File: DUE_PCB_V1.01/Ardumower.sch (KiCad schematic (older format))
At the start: 57 parts, among them J1 I2C_1, J10 P_Left, J11 P_Right, J12 Sonar_R, J13 Sonar_C, J14 Sonar_L, J15 Bumper, J16 Button, J17 Button, J18 Button, J19 Button, J2 I2C_2, J20 5V IN, J21 Remote, J22 PCB_2, J23 5V, J24 3.3V IN, J25 3.3V, J26 GND, J27 RX & TX, J3 I2C_3, J4 DS3231 RTC, J5 9V IN, J6 Drop_Left, J7 Drop_Right, J8 Tilt, J9 Rain

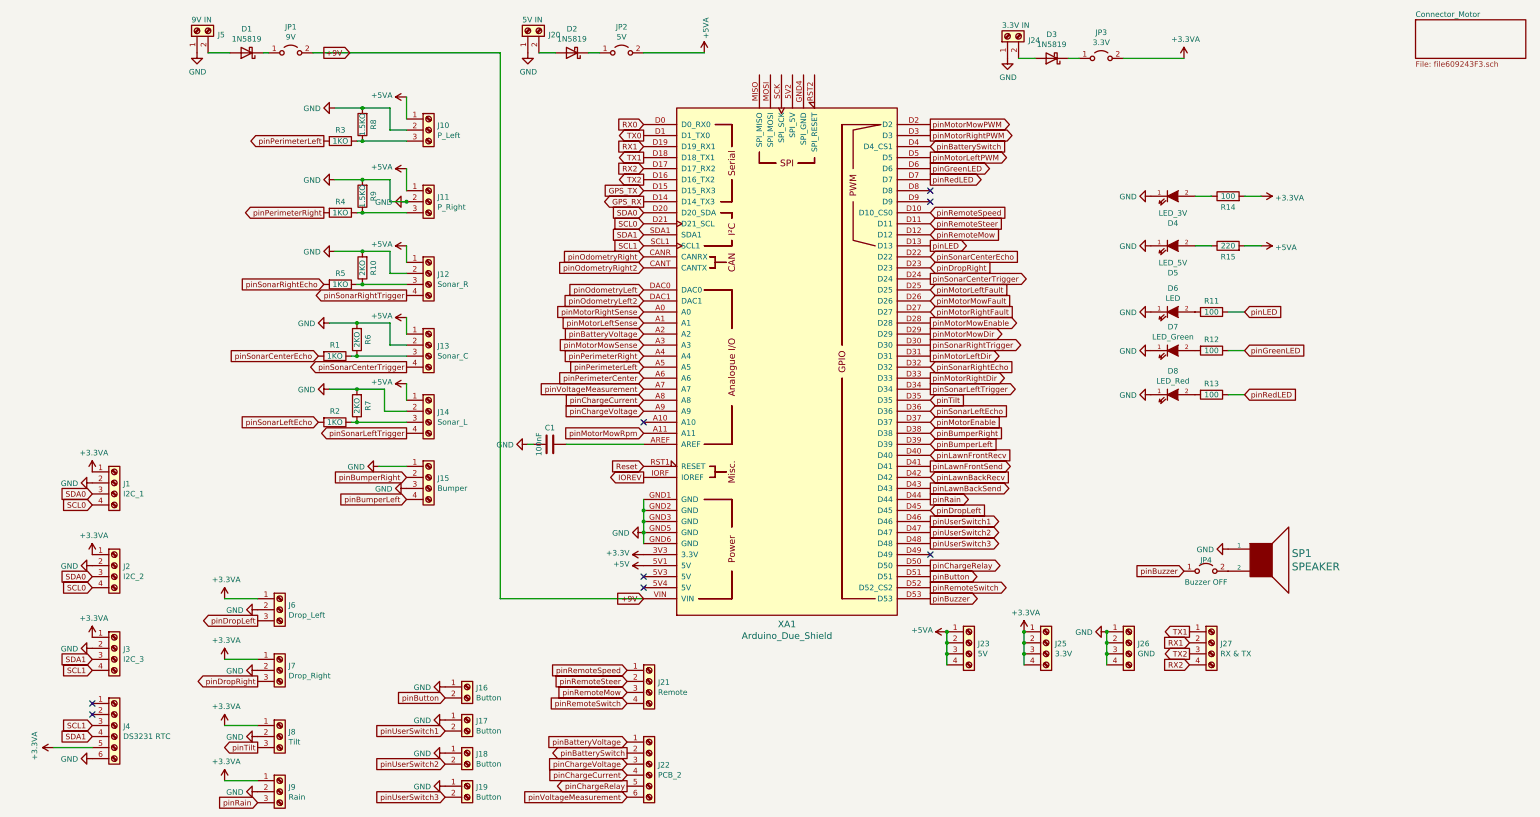
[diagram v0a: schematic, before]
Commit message: Add Power Connector for 5V and 3.3V
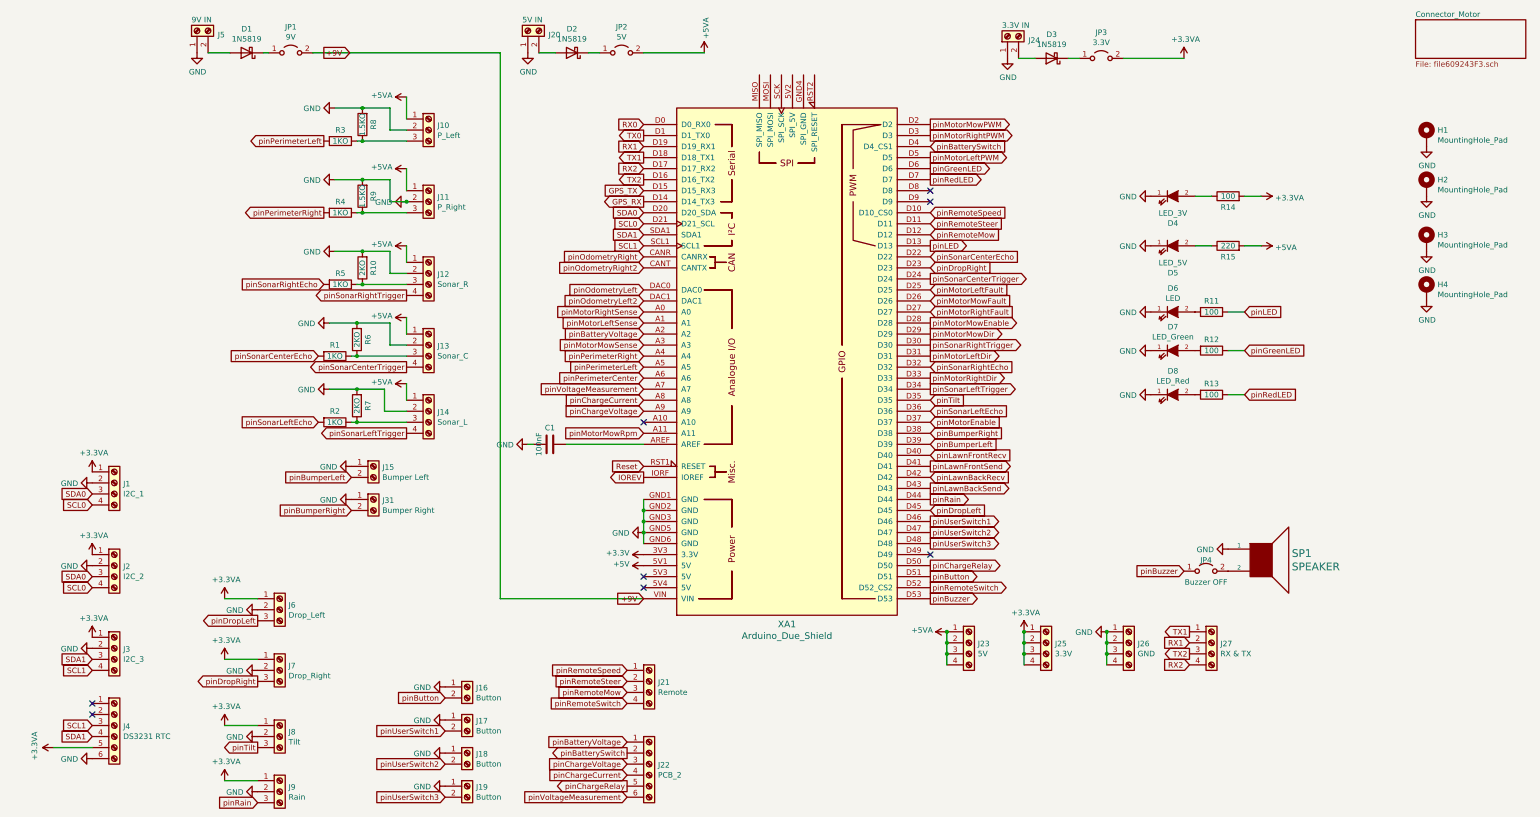
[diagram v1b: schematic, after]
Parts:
- removed J15: Bumper, Connector_PinHeader_2.54mm:PinHeader_1x04_P2.54mm_Vertical, symbol Connector:Screw_Terminal_01x04
- added H1, H2, H3, H4: MountingHole_Pad, MountingHole:MountingHole_2.2mm_M2_Pad_TopBottom, symbol Mechanical:MountingHole_Pad
- added J15: Bumper Left, Zimprich:Pin_Header_KK110_1x02_3D, symbol Connector:Screw_Terminal_01x02
- added J31: Bumper Right, Zimprich:Pin_Header_KK110_1x02_3D, symbol Connector:Screw_Terminal_01x02
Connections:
- net GND: now also H1.1, H2.1, H3.1, H4.1, J15.1 (Pin_1), J31.1 (Pin_1)
- net pinBumperLeft: now also J15.2 (Pin_2)
- net pinBumperRight: now also J31.2 (Pin_2)
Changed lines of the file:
@@
 Text GLabel 1900 4200 0    50   Input ~ 0
 pinSonarLeftEcho
-$Comp
-L Connector:Screw_Terminal_01x04 J15
-U 1 1 60770CE6
-P 2900 4700
-F 0 "J15" H 2980 4692 50  0000 L CNN
-F 1 "Bumper" H 2980 4601 50  0000 L CNN
-F 2 "Connector_PinHeader_2.54mm:PinHeader_1x04_P2.54mm_Vertical" H 2900 4700 50  0001 C CNN
-F 3 "~" H 2900 4700 50  0001 C CNN
-	1    2900 4700
-	1    0    0    -1
-$EndComp
-Text GLabel 2700 4700 0    50   Input ~ 0
+Text GLabel 2200 5000 0    50   Input ~ 0
 pinBumperRight
-Text GLabel 2700 4900 0    50   Input ~ 0
+Text GLabel 2200 4700 0    50   Input ~ 0
 pinBumperLeft
 $Comp
@@
 $EndComp
 $Comp
-L power:GND #PWR023
-U 1 1 6097EBFF
-P 2450 4600
-F 0 "#PWR023" H 2450 4350 50  0001 C CNN
-F 1 "GND" V 2455 4472 50  0000 R CNN
-F 2 "" H 2450 4600 50  0001 C CNN
-F 3 "" H 2450 4600 50  0001 C CNN
-	1    2450 4600
-	0    1    1    0
-$EndComp
-$Comp
 L power:GND #PWR018
 U 1 1 6097F3DC
@@
 	1    800  850
 	1    0    0    -1
-$EndComp
-Wire Wire Line
-	2450 4600 2700 4600
-$Comp
-L power:GND #PWR030
-U 1 1 609BE8A2
-P 2700 4800
-F 0 "#PWR030" H 2700 4550 50  0001 C CNN
-F 1 "GND" V 2705 4672 50  0000 R CNN
-F 2 "" H 2700 4800 50  0001 C CNN
-F 3 "" H 2700 4800 50  0001 C CNN
-	1    2700 4800
-	0    1    1    0
 $EndComp
 $Comp
@@
 	0    1    1    0
 $EndComp
+$Comp
+L Mechanical:MountingHole_Pad H2
+U 1 1 6091DE79
+P 11950 2050
+F 0 "H2" H 12050 2099 50  0000 L CNN
+F 1 "MountingHole_Pad" H 12050 2008 50  0000 L CNN
+F 2 "MountingHole:MountingHole_2.2mm_M2_Pad_TopBottom" H 11950 2050 50  0001 C CNN
+F 3 "~" H 11950 2050 50  0001 C CNN
+	1    11950 2050
+	1    0    0    -1
+$EndComp
+$Comp
+L power:GND #PWR055
+U 1 1 609238F5
+P 11950 2150
+F 0 "#PWR055" H 11950 1900 50  0001 C CNN
+F 1 "GND" H 11955 1977 50  0000 C CNN
+F 2 "" H 11950 2150 50  0001 C CNN
+F 3 "" H 11950 2150 50  0001 C CNN
+	1    11950 2150
+	1    0    0    -1
+$EndComp
+$Comp
+L Mechanical:MountingHole_Pad H1
+U 1 1 6092EAEB
+P 11950 1600
+F 0 "H1" H 12050 1649 50  0000 L CNN
+F 1 "MountingHole_Pad" H 12050 1558 50  0000 L CNN
+F 2 "MountingHole:MountingHole_2.2mm_M2_Pad_TopBottom" H 11950 1600 50  0001 C CNN
+F 3 "~" H 11950 1600 50  0001 C CNN
+	1    11950 1600
+	1    0    0    -1
+$EndComp
+$Comp
+L power:GND #PWR054
+U 1 1 6092F555
+P 11950 1700
+F 0 "#PWR054" H 11950 1450 50  0001 C CNN
+F 1 "GND" H 11955 1527 50  0000 C CNN
+F 2 "" H 11950 1700 50  0001 C CNN
+F 3 "" H 11950 1700 50  0001 C CNN
+	1    11950 1700
+	1    0    0    -1
+$EndComp
+$Comp
+L Mechanical:MountingHole_Pad H4
+U 1 1 609317B3
+P 11950 3000
+F 0 "H4" H 12050 3049 50  0000 L CNN
+F 1 "MountingHole_Pad" H 12050 2958 50  0000 L CNN
+F 2 "MountingHole:MountingHole_2.2mm_M2_Pad_TopBottom" H 11950 3000 50  0001 C CNN
+F 3 "~" H 11950 3000 50  0001 C CNN
+	1    11950 3000
+	1    0    0    -1
+$EndComp
+$Comp
+L power:GND #PWR057
+U 1 1 60932237
+P 11950 3100
+F 0 "#PWR057" H 11950 2850 50  0001 C CNN
+F 1 "GND" H 11955 2927 50  0000 C CNN
+F 2 "" H 11950 3100 50  0001 C CNN
+F 3 "" H 11950 3100 50  0001 C CNN
+	1    11950 3100
+	1    0    0    -1
+$EndComp
+$Comp
+L Mechanical:MountingHole_Pad H3
+U 1 1 60932241
+P 11950 2550
+F 0 "H3" H 12050 2599 50  0000 L CNN
+F 1 "MountingHole_Pad" H 12050 2508 50  0000 L CNN
+F 2 "MountingHole:MountingHole_2.2mm_M2_Pad_TopBottom" H 11950 2550 50  0001 C CNN
+F 3 "~" H 11950 2550 50  0001 C CNN
+	1    11950 2550
+	1    0    0    -1
+$EndComp
+$Comp
+L power:GND #PWR056
+U 1 1 6093224B
+P 11950 2650
+F 0 "#PWR056" H 11950 2400 50  0001 C CNN
+F 1 "GND" H 11955 2477 50  0000 C CNN
+F 2 "" H 11950 2650 50  0001 C CNN
+F 3 "" H 11950 2650 50  0001 C CNN
+	1    11950 2650
+	1    0    0    -1
+$EndComp
+$Comp
+L Connector:Screw_Terminal_01x02 J15
+U 1 1 609D47E3
+P 2400 4600
+F 0 "J15" H 2480 4592 50  0000 L CNN
+F 1 "Bumper Left" H 2480 4501 50  0000 L CNN
+F 2 "Zimprich:Pin_Header_KK110_1x02_3D" H 2400 4600 50  0001 C CNN
+F 3 "~" H 2400 4600 50  0001 C CNN
+	1    2400 4600
+	1    0    0    -1
+$EndComp
+$Comp
+L power:GND #PWR023
+U 1 1 609D52AA
+P 2200 4600
+F 0 "#PWR023" H 2200 4350 50  0001 C CNN
+F 1 "GND" V 2205 4472 50  0000 R CNN
+F 2 "" H 2200 4600 50  0001 C CNN
+F 3 "" H 2200 4600 50  0001 C CNN
+	1    2200 4600
+	0    1    1    0
+$EndComp
+$Comp
+L Connector:Screw_Terminal_01x02 J31
+U 1 1 609DA7EE
+P 2400 4900
+F 0 "J31" H 2480 4892 50  0000 L CNN
+F 1 "Bumper Right" H 2480 4801 50  0000 L CNN
+F 2 "Zimprich:Pin_Header_KK110_1x02_3D" H 2400 4900 50  0001 C CNN
+F 3 "~" H 2400 4900 50  0001 C CNN
+	1    2400 4900
+	1    0    0    -1
+$EndComp
+$Comp
+L power:GND #PWR030
+U 1 1 609DA7F8
+P 2200 4900
+F 0 "#PWR030" H 2200 4650 50  0001 C CNN
+F 1 "GND" V 2205 4772 50  0000 R CNN
+F 2 "" H 2200 4900 50  0001 C CNN
+F 3 "" H 2200 4900 50  0001 C CNN
+	1    2200 4900
+	0    1    1    0
+$EndComp

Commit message: Ad new RX TX Connector and some other improvements
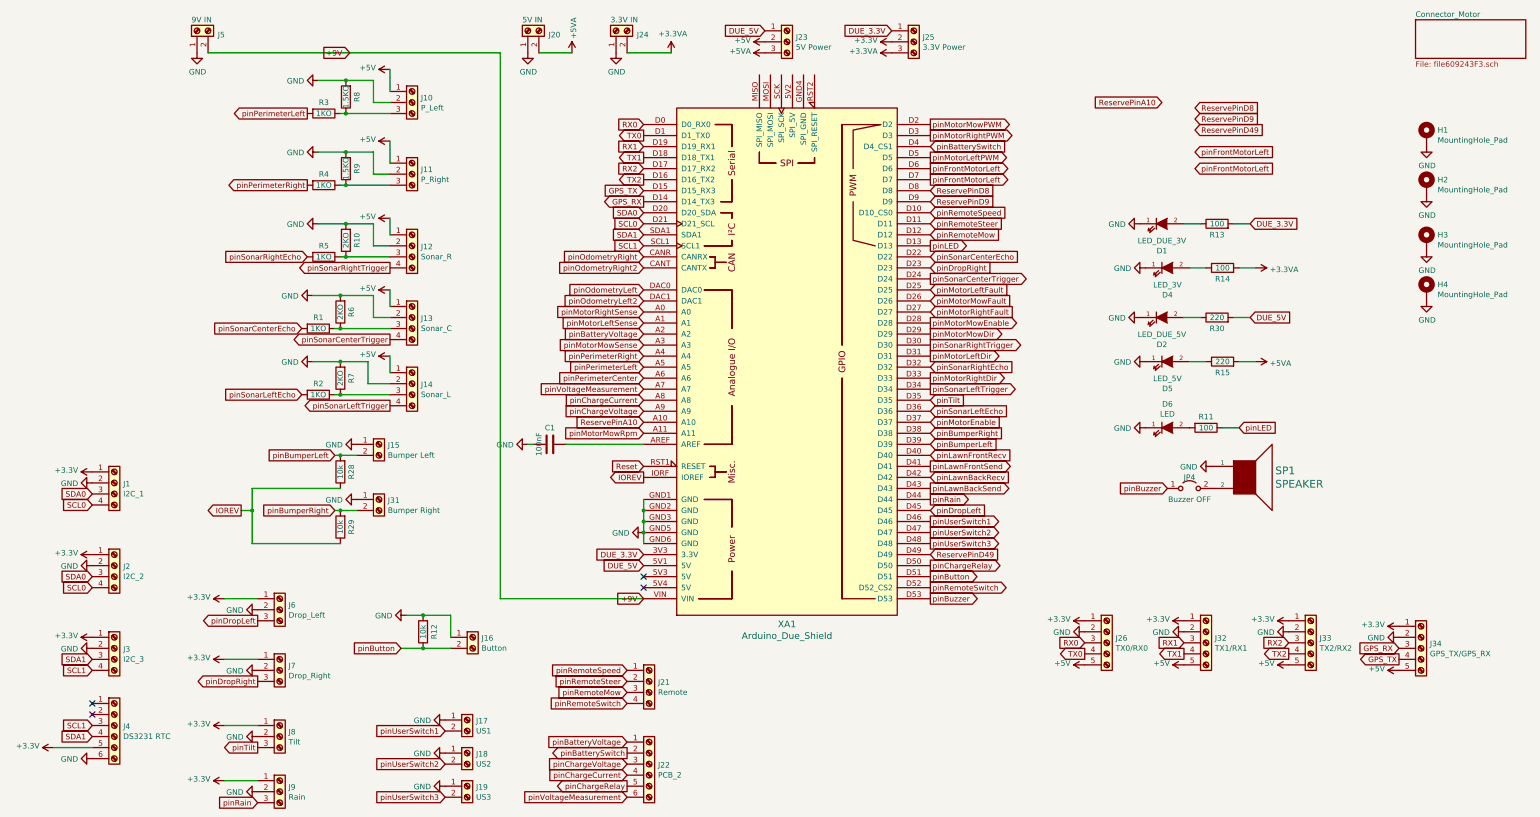
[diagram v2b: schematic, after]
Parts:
- removed D1, D2, D3: 1N5819, Diode_THT:D_DO-41_SOD81_P10.16mm_Horizontal, symbol Diode:1N5819
- removed D7: LED_Green, LED_THT:LED_D3.0mm, symbol Zimprich:LED
- removed D8: LED_Red, LED_THT:LED_D3.0mm, symbol Zimprich:LED
- removed J23: 5V, Connector_PinHeader_2.54mm:PinHeader_1x04_P2.54mm_Vertical, symbol Connector:Screw_Terminal_01x04
- removed J25: 3.3V, Connector_PinHeader_2.54mm:PinHeader_1x04_P2.54mm_Vertical, symbol Connector:Screw_Terminal_01x04
- removed J26: GND, Connector_PinHeader_2.54mm:PinHeader_1x04_P2.54mm_Vertical, symbol Connector:Screw_Terminal_01x04
- removed J27: RX & TX, Connector_PinHeader_2.54mm:PinHeader_1x04_P2.54mm_Vertical, symbol Connector:Screw_Terminal_01x04
- removed JP1: 9V, Connector_PinHeader_2.54mm:PinHeader_1x02_P2.54mm_Vertical, symbol Jumper:Jumper_2_Open
- removed JP2: 5V, Connector_PinHeader_2.54mm:PinHeader_1x02_P2.54mm_Vertical, symbol Jumper:Jumper_2_Open
- removed JP3: 3.3V, Connector_PinHeader_2.54mm:PinHeader_1x02_P2.54mm_Vertical, symbol Jumper:Jumper_2_Open
- added D1: LED_DUE_3V, LED_THT:LED_D3.0mm, symbol Zimprich:LED
- added D2: LED_DUE_5V, LED_THT:LED_D3.0mm, symbol Zimprich:LED
- added J23: 5V Power, Connector_PinHeader_2.54mm:PinHeader_1x03_P2.54mm_Vertical, symbol Connector:Screw_Terminal_01x03
- added J25: 3.3V Power, Connector_PinHeader_2.54mm:PinHeader_1x03_P2.54mm_Vertical, symbol Connector:Screw_Terminal_01x03
- added J26: TX0/RX0, Connector_PinHeader_2.54mm:PinHeader_1x05_P2.54mm_Horizontal, symbol Connector:Screw_Terminal_01x05
- added J32: TX1/RX1, Connector_PinHeader_2.54mm:PinHeader_1x05_P2.54mm_Vertical, symbol Connector:Screw_Terminal_01x05
- added J33: TX2/RX2, Connector_PinHeader_2.54mm:PinHeader_1x05_P2.54mm_Vertical, symbol Connector:Screw_Terminal_01x05
- added J34: GPS_TX/GPS_RX, Connector_PinHeader_2.54mm:PinHeader_1x05_P2.54mm_Vertical, symbol Connector:Screw_Terminal_01x05
- added R28, R29: 10k, Resistor_THT:R_Axial_DIN0207_L6.3mm_D2.5mm_P2.54mm_Vertical, symbol Device:R
- added R30: 220, Resistor_THT:R_Axial_DIN0207_L6.3mm_D2.5mm_P2.54mm_Vertical, symbol Device:R
- J17: value Button -> US1
- J18: value Button -> US2
- J19: value Button -> US3
- R12: value 100 -> 10k
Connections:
- net +3.3VA: now also J24.2 (Pin_2), J25.3 (Pin_3); no longer J1.1 (Pin_1), J2.1 (Pin_1), J3.1 (Pin_1), J4.5 (Pin_5), J6.1 (Pin_1), J7.1 (Pin_1), J8.1 (Pin_1), J9.1 (Pin_1)
- net +3V3: now also J1.1 (Pin_1), J2.1 (Pin_1), J3.1 (Pin_1), J4.5 (Pin_5), J6.1 (Pin_1), J7.1 (Pin_1), J8.1 (Pin_1), J9.1 (Pin_1), J25.2 (Pin_2), J26.1 (Pin_1), J32.1 (Pin_1), J33.1 (Pin_1), J34.1 (Pin_1); no longer XA1.3V3 (3.3V)
- net +5V: now also J10.1 (Pin_1), J11.1 (Pin_1), J12.1 (Pin_1), J13.1 (Pin_1), J14.1 (Pin_1), J23.2 (Pin_2), J26.5 (Pin_5), J32.5 (Pin_5), J33.5 (Pin_5), J34.5 (Pin_5); no longer XA1.5V1 (5V)
- net +5VA: now also J20.2 (Pin_2), J23.3 (Pin_3); no longer J10.1 (Pin_1), J11.1 (Pin_1), J12.1 (Pin_1), J13.1 (Pin_1), J14.1 (Pin_1)
- net +9V: now also J5.2 (Pin_2)
- net GND: now also R12.2, D1.1 (K), D2.1 (K), J26.2 (Pin_2), J32.2 (Pin_2), J33.2 (Pin_2), J34.2 (Pin_2)
- net GPS_RX: now also J34.3 (Pin_3)
- net GPS_TX: now also J34.4 (Pin_4)
- net IOREV: now also R28.1, R29.1
- net RX0: now also J26.3 (Pin_3)
- net RX1: now also J32.3 (Pin_3)
- net RX2: now also J33.3 (Pin_3)
- net TX0: now also J26.4 (Pin_4)
- net TX1: now also J32.4 (Pin_4)
- net TX2: now also J33.4 (Pin_4)
- net pinBumperLeft: now also R28.2
- net pinBumperRight: now also R29.2
- net pinButton: now also R12.1
- net ReservePinA10: now reaches XA1.A10
- net ReservePinD49: now reaches XA1.D49
- net ReservePinD8: now reaches XA1.D8
- net ReservePinD9: now reaches XA1.D9
- net DUE_3.3V: now reaches R13.2
- net DUE_3.3V: now also XA1.3V3 (3.3V), J25.1 (Pin_1)
- net pinGreenLED renamed pinFrontMotorLeft
- net pinFrontMotorLeft: now also XA1.D7; no longer R12.1
- net pinRedLED: no longer names the net of R13.1
- net pinRedLED: now also D1.2 (A); no longer XA1.D7
- new net: D2.2 (A), R30.1
- new net DUE_5V: J23.1 (Pin_1), R30.2, XA1.5V1 (5V)
- no-connect marks 8 -> 4
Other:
- moved on the sheet: D4, D5, D6, J10, J11, J12, J13, J14, J15, J16, J24, J31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

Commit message: Change Connector Type
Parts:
- J15: footprint Zimprich:Pin_Header_KK110_1x02_3D -> Connector_PinHeader_2.54mm:PinHeader_1x02_P2.54mm_Vertical
- J26: footprint Connector_PinHeader_2.54mm:PinHeader_1x05_P2.54mm_Horizontal -> Connector_PinHeader_2.54mm:PinHeader_1x05_P2.54mm_Vertical
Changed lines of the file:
@@
 F 0 "J15" H 2530 4392 50  0000 L CNN
 F 1 "Bumper Left" H 2530 4301 50  0000 L CNN
-F 2 "Zimprich:Pin_Header_KK110_1x02_3D" H 2450 4400 50  0001 C CNN
+F 2 "Connector_PinHeader_2.54mm:PinHeader_1x02_P2.54mm_Vertical" H 2450 4400 50  0001 C CNN
 F 3 "~" H 2450 4400 50  0001 C CNN
 	1    2450 4400
@@
 F 0 "J26" H 9130 6242 50  0000 L CNN
 F 1 "TX0/RX0" H 9130 6151 50  0000 L CNN
-F 2 "Connector_PinHeader_2.54mm:PinHeader_1x05_P2.54mm_Horizontal" H 9050 6200 50  0001 C CNN
+F 2 "Connector_PinHeader_2.54mm:PinHeader_1x05_P2.54mm_Vertical" H 9050 6200 50  0001 C CNN
 F 3 "~" H 9050 6200 50  0001 C CNN
 	1    9050 6200
